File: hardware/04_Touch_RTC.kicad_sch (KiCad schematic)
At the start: 23 parts, among them J7 FH12-6S-0.5SH(55) TOUCH, U11 TPS7A0230PDBVR, U12 SN74LVC1G07QDBVRQ1, U13 SN74LVC1G74-Q1 WAKE LATCH OPT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, U14 RV-3028-C7

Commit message: Rebuild phase 2 schematic by function
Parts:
- added TP30: I2C_SDA, TestPoint:TestPoint_Pad_D1.0mm, symbol LandyHeater:I2C_SDA_11
- added TP31: I2C_SCL, TestPoint:TestPoint_Pad_D1.0mm, symbol LandyHeater:I2C_SCL_11
- added TP32: TOUCH_INT_N, TestPoint:TestPoint_Pad_D1.0mm, symbol LandyHeater:TOUCH_INT_N_11
- added TP33: TOUCH_RESET_N, TestPoint:TestPoint_Pad_D1.0mm, symbol LandyHeater:TOUCH_RESET_N_11
- U14: Notes (none) -> PROVISIONAL project-local footprint; verify against current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
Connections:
- net I2C_SCL: now also TP31.1
- net I2C_SDA: now also TP30.1
- net TOUCH_INT_N: now also TP32.1
- net TOUCH_RESET_N: now also TP33.1
- net RTC_VBACKUP: no longer names the net of D6.3 (K), U14.6 (VBACKUP)
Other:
- note added: "3V0 TOUCH ALWAYS-ON / I2C"
- note added: "DIRECT TOUCH WAKE (DEFAULT)"
- note added: "FLOW: 3V3 -> TPS7A02 -> TOUCH + I2C PULL-UPS | TOUCH INT -> GPIO2 WAKE"
- note added: "RTC + PRIMARY CELL — internal trickle charger must remain disabled"
- note added: "WAKE LATCH OPTION — ALL PARTS DNP; mutually exclusive with direct path"
- moved on the sheet: BT1, C28, C29, C30, C39, D6, J7, R24, R25, R26, R27, R28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

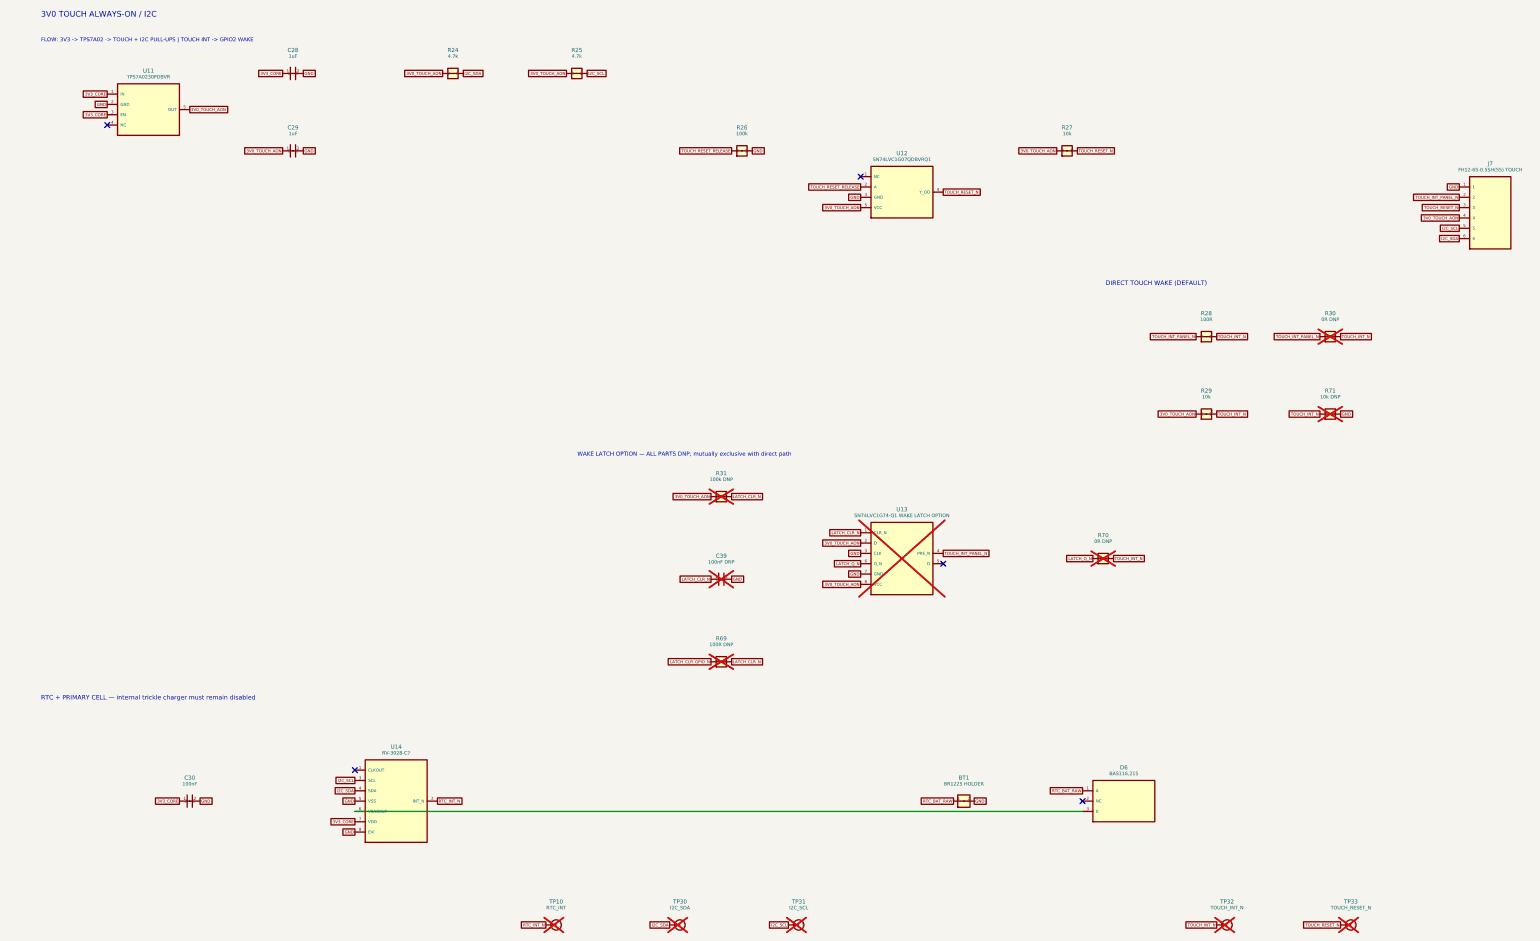
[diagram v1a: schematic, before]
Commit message: Redraw phase 2 schematic with visible functional wiring
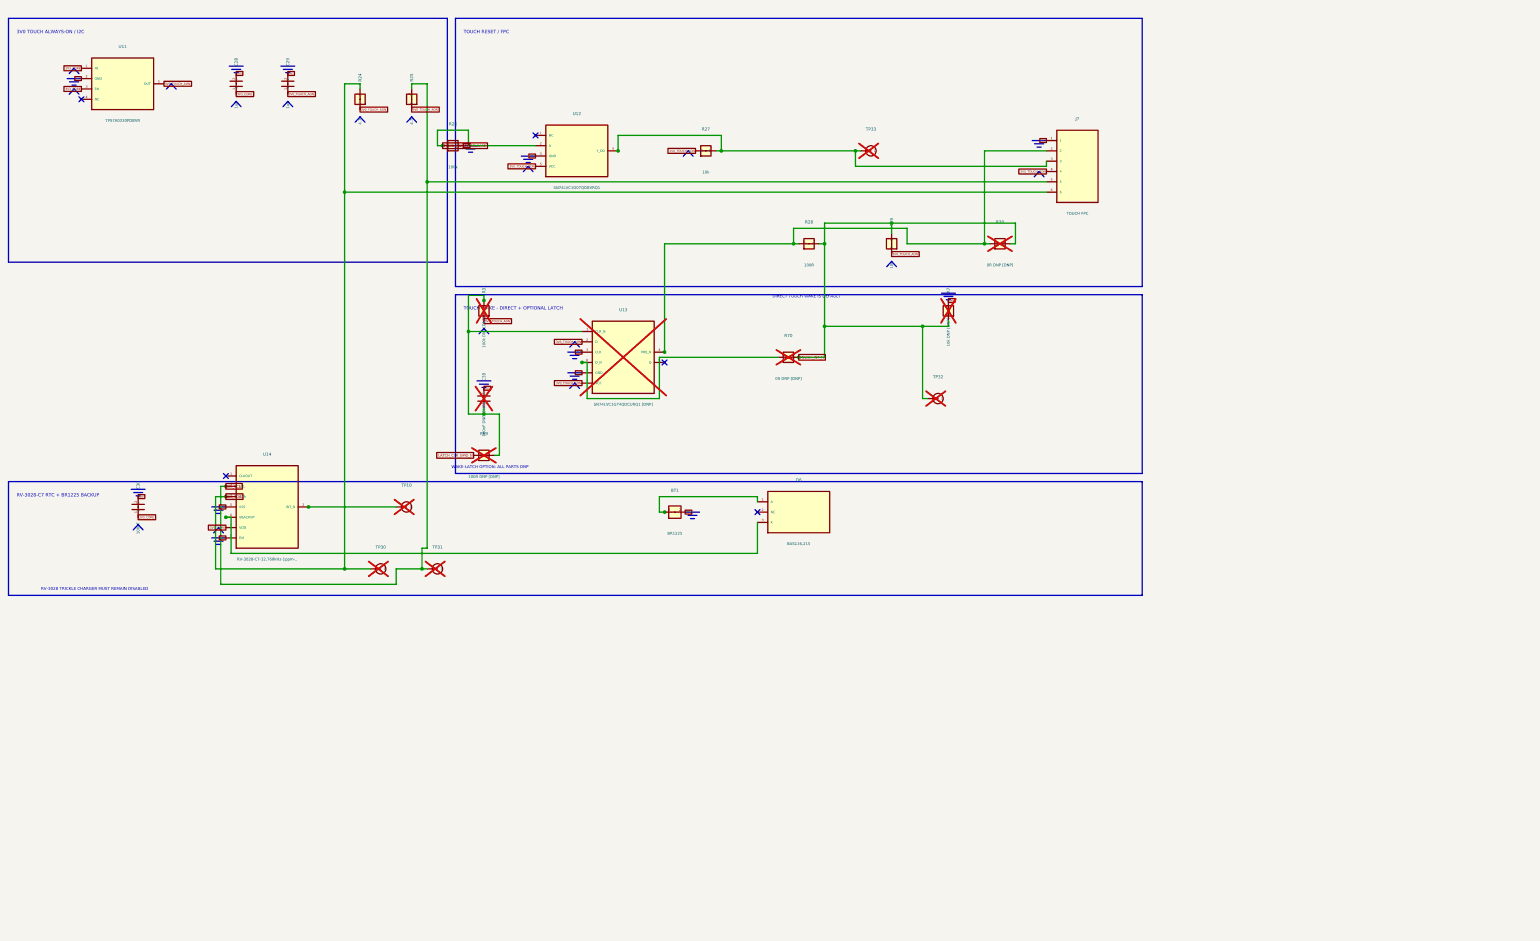
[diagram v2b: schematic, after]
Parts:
- BT1: Circuit label (none) -> BR1225
- C28, C29: Circuit label (none) -> 1uF
- C30: Circuit label (none) -> 100nF
- C39: Circuit label (none) -> 100nF DNP [DNP]
- D6: Circuit label (none) -> BAS116,215
- J7: Circuit label (none) -> TOUCH FPC
- R24, R25: Circuit label (none) -> 4.7k
- R26: Circuit label (none) -> 100k
- R27, R29: Circuit label (none) -> 10k
- R28: Circuit label (none) -> 100R
- R30, R70: Circuit label (none) -> 0R DNP [DNP]
- R31: Circuit label (none) -> 100k DNP [DNP]
- R69: Circuit label (none) -> 100R DNP [DNP]
- R71: Circuit label (none) -> 10k DNP [DNP]
- U11: Circuit label (none) -> TPS7A0230PDBVR
- U12: Circuit label (none) -> SN74LVC1G07QDBVRQ1
- U13: Circuit label (none) -> SN74LVC1G74QDCURQ1 [DNP]
- U14: Circuit label (none) -> RV-3028-C7-32.768kHz-1ppm-..
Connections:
- net LATCH_CLR_N: no longer names the net of C39.1, R31.2, R69.2, U13.1 (CLR_N)
- net LATCH_Q_N: no longer names the net of R70.1, U13.6 (Q_N)
- net RTC_BAT_RAW: no longer names the net of BT1.1 (+), D6.1 (A)
- net RTC_INT_N: no longer names the net of TP10.1, U14.2 (INT_N)
- net TOUCH_INT_PANEL_N: no longer names the net of J7.2, R28.1, R30.1, U13.4 (PRE_N)
- net TOUCH_RESET_N: no longer names the net of J7.3, R27.2, TP33.1, U12.4 (Y_OD)
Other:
- note added: "DIRECT TOUCH WAKE IS DEFAULT"
- note added: "RV-3028 TRICKLE CHARGER MUST REMAIN DISABLED"
- note added: "RV-3028-C7 RTC + BR1225 BACKUP"
- note added: "TOUCH RESET / FPC"
- note added: "TOUCH WAKE - DIRECT + OPTIONAL LATCH"
- note added: "WAKE-LATCH OPTION: ALL PARTS DNP"
- note removed: "DIRECT TOUCH WAKE (DEFAULT)"
- note removed: "FLOW: 3V3 -> TPS7A02 -> TOUCH + I2C PULL-UPS | TOUCH INT -> GPIO2 WAKE"
- note removed: "RTC + PRIMARY CELL — internal trickle charger must remain disabled"
- note removed: "WAKE LATCH OPTION — ALL PARTS DNP; mutually exclusive with direct path"
- moved on the sheet: BT1, C28, C29, C30, C39, D6, J7, R24, R25, R26, R27, R28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
